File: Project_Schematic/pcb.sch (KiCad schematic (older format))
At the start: 36 parts, among them J1 USB_microB_2040002-1, Q1 2N2219, U1 FT232RQ, U2 MCP1702T-5002E_CB, U3 TPS2113ADRBR, U4 ATMEGA328PB-MNR, U5 VibratingMotor, U6 BT_HC05, Y1 16MHz

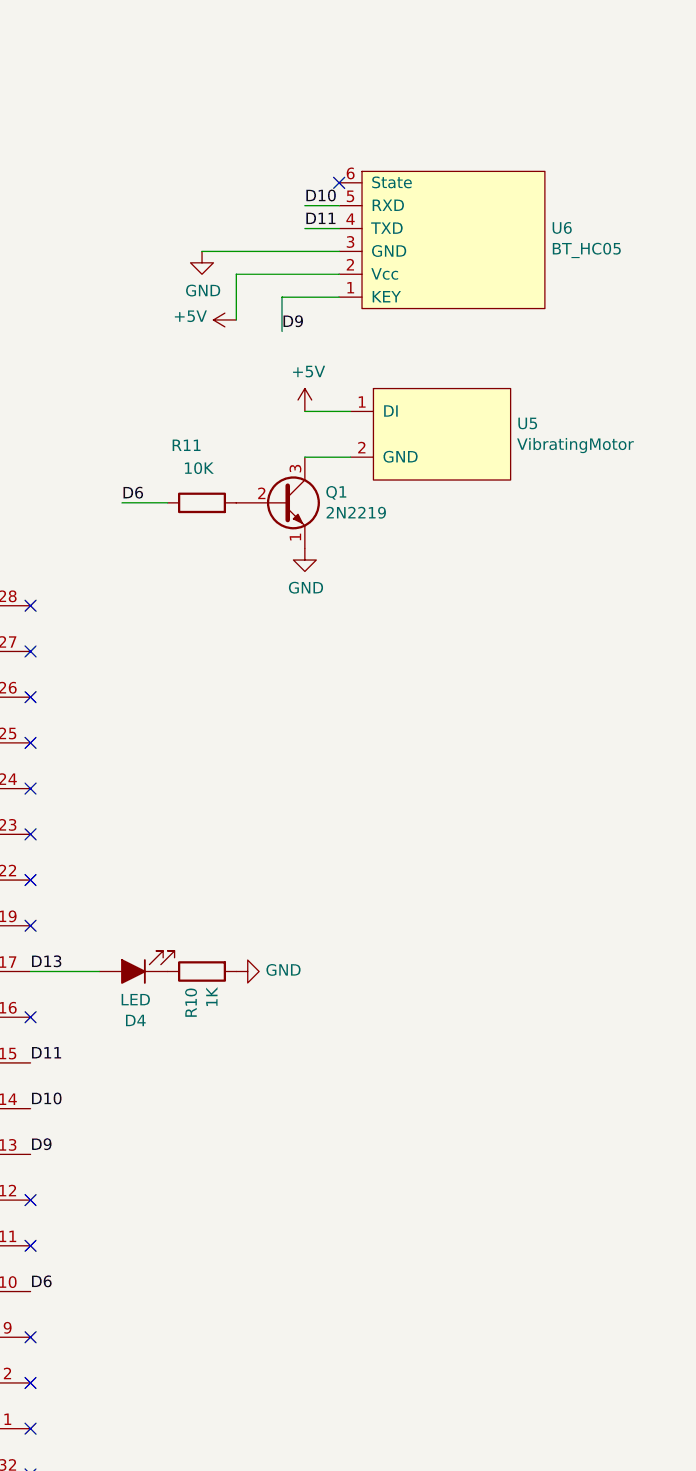
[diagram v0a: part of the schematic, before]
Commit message: modifying circuit for pcb
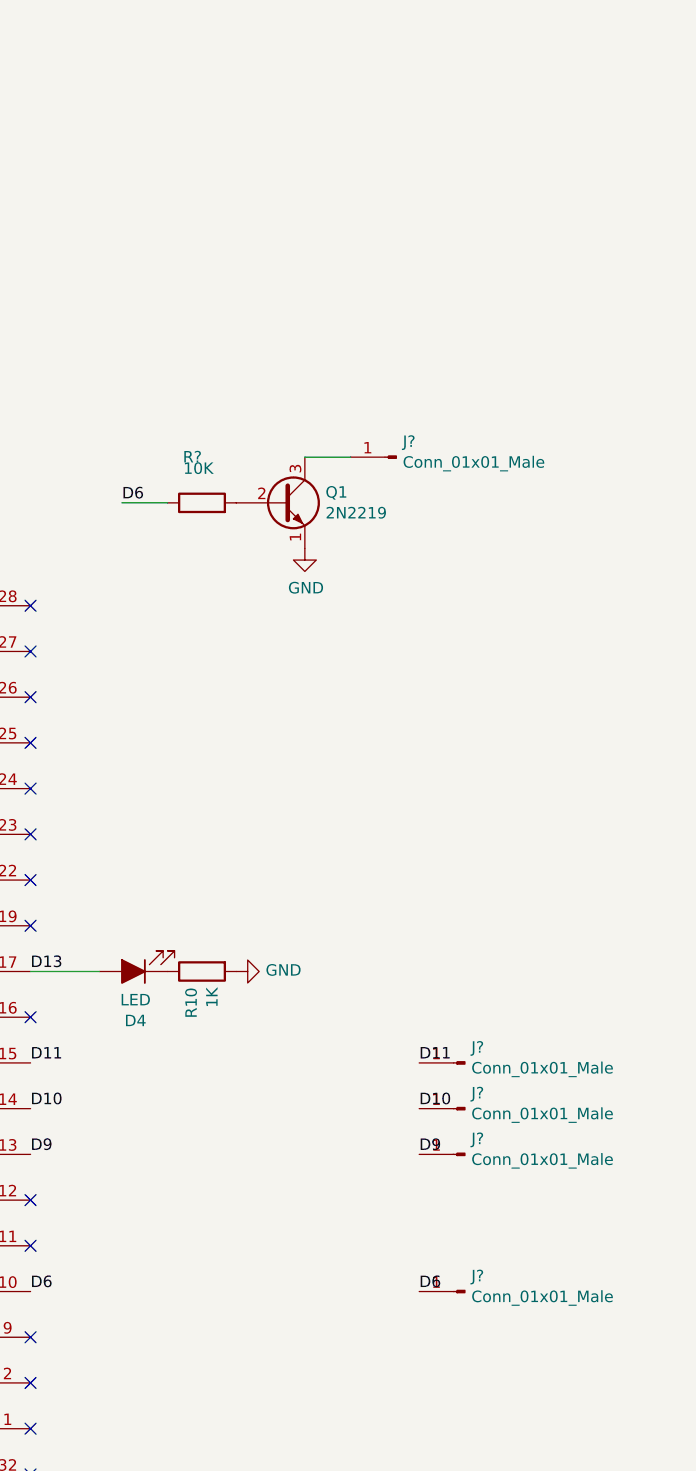
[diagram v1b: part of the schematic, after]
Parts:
- removed U5: VibratingMotor, symbol PoE:VibratingMotor
- removed U6: BT_HC05, symbol PoE:BT_HC05
- added J? (x5): Conn_01x01_Male, symbol Connector:Conn_01x01_Male
- renumbered R11 to R?
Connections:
- net D10: now also J?.1 (Pin_1)
- net D11: now also J?.1 (Pin_1)
- net D6: now also J?.1 (Pin_1)
- net D9: now also J?.1 (Pin_1)
- net at Q1.3 (C): now also J?.1 (Pin_1)
- no-connect marks 41 -> 40
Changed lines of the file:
@@
 	0    1    1    0
-$EndComp
-$Comp
-L PoE:BT_HC05 U6
-U 1 1 5DBAA234
-P 12950 2550
-F 0 "U6" H 13178 2551 50  0000 L CNN
-F 1 "BT_HC05" H 13178 2460 50  0000 L CNN
-F 2 "" H 11900 3150 50  0001 C CNN
-F 3 "" H 11900 3150 50  0001 C CNN
-	1    12950 2550
-	1    0    0    -1
-$EndComp
-Text Label 12100 2450 0    50   ~ 0
-D10
-Wire Wire Line
-	12250 2450 12100 2450
-Text Label 12100 2550 0    50   ~ 0
-D11
-Wire Wire Line
-	12100 2550 12250 2550
-$Comp
-L power:GND #PWR040
-U 1 1 5DBC74CB
-P 11650 2650
-F 0 "#PWR040" H 11650 2400 50  0001 C CNN
-F 1 "GND" H 11655 2477 50  0000 C CNN
-F 2 "" H 11650 2650 50  0001 C CNN
-F 3 "" H 11650 2650 50  0001 C CNN
-	1    11650 2650
-	1    0    0    -1
-$EndComp
-Wire Wire Line
-	12250 2650 11650 2650
-$Comp
-L power:+5V #PWR041
-U 1 1 5DBAA379
-P 11800 2950
-F 0 "#PWR041" H 11800 2800 50  0001 C CNN
-F 1 "+5V" V 11815 3078 50  0000 L CNN
-F 2 "" H 11800 2950 50  0001 C CNN
-F 3 "" H 11800 2950 50  0001 C CNN
-	1    11800 2950
-	0    -1   -1   0
-$EndComp
-Wire Wire Line
-	12250 2750 11800 2750
-Wire Wire Line
-	11800 2750 11800 2950
-NoConn ~ 12250 2350
-$Comp
-L PoE:VibratingMotor U5
-U 1 1 5DBD8115
-P 12700 3450
-F 0 "U5" H 13028 3496 50  0000 L CNN
-F 1 "VibratingMotor" H 13028 3405 50  0000 L CNN
-F 2 "" H 12150 3650 50  0001 C CNN
-F 3 "" H 12150 3650 50  0001 C CNN
-	1    12700 3450
-	1    0    0    -1
 $EndComp
 Wire Wire Line
 	12100 3550 12300 3550
-Wire Wire Line
-	12100 3350 12300 3350
-Text Label 12000 3000 0    50   ~ 0
-D9
-Wire Wire Line
-	12000 3000 12000 2850
-Wire Wire Line
-	12000 2850 12250 2850
 $Comp
 L power:GND #PWR043
@@
 	1    0    0    -1
 $EndComp
-$Comp
-L power:+5V #PWR042
-U 1 1 5DBE7AB2
-P 12100 3350
-F 0 "#PWR042" H 12100 3200 50  0001 C CNN
-F 1 "+5V" H 12115 3523 50  0000 C CNN
-F 2 "" H 12100 3350 50  0001 C CNN
-F 3 "" H 12100 3350 50  0001 C CNN
-	1    12100 3350
-	1    0    0    -1
-$EndComp
 Text Label 11300 3750 0    50   ~ 0
 D6
 Wire Wire Line
 	11300 3750 11500 3750
-$Comp
-L Device:R R11
-U 1 1 5DC4498E
-P 11650 3750
-F 0 "R11" V 11900 3750 50  0000 L CNN
-F 1 "10K" V 11800 3700 50  0000 L CNN
-F 2 "Resistor_SMD:R_0603_1608Metric" V 11580 3750 50  0001 C CNN
-F 3 "~" H 11650 3750 50  0001 C CNN
-	1    11650 3750
-	0    -1   -1   0
-$EndComp
 $Comp
 L Transistor_BJT:2N2219 Q1
@@
 Text Label 10900 6200 0    50   ~ 0
 D11
+$Comp
+L Device:R R?
+U 1 1 5DC4498E
+P 11650 3750
+F 0 "R?" V 11850 3750 50  0000 L CNN
+F 1 "10K" V 11800 3700 50  0000 L CNN
+F 2 "Resistor_SMD:R_0603_1608Metric" V 11580 3750 50  0001 C CNN
+F 3 "~" H 11650 3750 50  0001 C CNN
+	1    11650 3750
+	0    -1   -1   0
+$EndComp
+$Comp
+L Connector:Conn_01x01_Male J?
+U 1 1 5DE2172C
+P 12800 7200
+F 0 "J?" H 12772 7132 50  0000 R CNN
+F 1 "Conn_01x01_Male" H 12772 7223 50  0000 R CNN
+F 2 "" H 12800 7200 50  0001 C CNN
+F 3 "~" H 12800 7200 50  0001 C CNN
+	1    12800 7200
+	-1   0    0    1
+$EndComp
+Text Label 12600 7200 0    50   ~ 0
+D6
+NoConn ~ 10900 8000
+NoConn ~ 10900 7800
+NoConn ~ 10900 7600
+NoConn ~ 10900 7400
+NoConn ~ 10900 7000
+NoConn ~ 10900 6800
+NoConn ~ 10900 6000
+NoConn ~ 10900 5600
+NoConn ~ 10900 5400
+NoConn ~ 10900 5200
+NoConn ~ 10900 5000
+NoConn ~ 10900 4800
+NoConn ~ 10900 4600
+NoConn ~ 10900 4400
 NoConn ~ 10900 4200
-NoConn ~ 10900 4400
-NoConn ~ 10900 4600
-NoConn ~ 10900 4800
-NoConn ~ 10900 5000
-NoConn ~ 10900 5200
-NoConn ~ 10900 5400
-NoConn ~ 10900 5600
-NoConn ~ 10900 6000
-NoConn ~ 10900 6800
-NoConn ~ 10900 7000
-NoConn ~ 10900 7400
-NoConn ~ 10900 7600
-NoConn ~ 10900 7800
-NoConn ~ 10900 8000
+$Comp
+L Connector:Conn_01x01_Male J?
+U 1 1 5DE5E436
+P 12800 6600
+F 0 "J?" H 12772 6532 50  0000 R CNN
+F 1 "Conn_01x01_Male" H 12772 6623 50  0000 R CNN
+F 2 "" H 12800 6600 50  0001 C CNN
+F 3 "~" H 12800 6600 50  0001 C CNN
+	1    12800 6600
+	-1   0    0    1
+$EndComp
+$Comp
+L Connector:Conn_01x01_Male J?
+U 1 1 5DE5FF58
+P 12800 6400
+F 0 "J?" H 12772 6332 50  0000 R CNN
+F 1 "Conn_01x01_Male" H 12772 6423 50  0000 R CNN
+F 2 "" H 12800 6400 50  0001 C CNN
+F 3 "~" H 12800 6400 50  0001 C CNN
+	1    12800 6400
+	-1   0    0    1
+$EndComp
+$Comp
+L Connector:Conn_01x01_Male J?
+U 1 1 5DE61393
+P 12800 6200
+F 0 "J?" H 12772 6132 50  0000 R CNN
+F 1 "Conn_01x01_Male" H 12772 6223 50  0000 R CNN
+F 2 "" H 12800 6200 50  0001 C CNN
+F 3 "~" H 12800 6200 50  0001 C CNN
+	1    12800 6200
+	-1   0    0    1
+$EndComp
+Text Label 12600 6600 0    50   ~ 0
+D9
+Text Label 12600 6400 0    50   ~ 0
+D10
+Text Label 12600 6200 0    50   ~ 0
+D11
+$Comp
+L Connector:Conn_01x01_Male J?
+U 1 1 5DE83073
+P 12500 3550
+F 0 "J?" H 12472 3482 50  0000 R CNN
+F 1 "Conn_01x01_Male" H 12472 3573 50  0000 R CNN
+F 2 "" H 12500 3550 50  0001 C CNN
+F 3 "~" H 12500 3550 50  0001 C CNN
+	1    12500 3550
+	-1   0    0    1
+$EndComp
 $EndSCHEMATC
